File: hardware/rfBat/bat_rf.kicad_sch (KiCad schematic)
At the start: 98 parts, among them J1 USB_C_Receptacle_PowerOnly_6P, J2 Conn_01x02_Socket, J4 Conn_01x03, Q1 NMOS, Q2 PMOS, Q3 NMOS, Q4 KNY3406C, SW1 3*4*2.5MM_贴片4脚, SW3 SW_MEC_5E, U1 ESP32-C3-WROOM-02-N4, U2 IP2325_5M_WHJC, U3 SPX3819M5-L-3-3, U4 AMS1117

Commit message: update rfBat pcb
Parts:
- removed D1: BAT54C, Package_TO_SOT_SMD:SOT-23, symbol Diode:BAT54C
- removed Q1, Q3: NMOS, Package_TO_SOT_SMD:SOT-23, symbol Simulation_SPICE:NMOS
- removed Q2: PMOS, Package_TO_SOT_SMD:SOT-23, symbol Simulation_SPICE:PMOS
- removed SW3: SW_MEC_5E, bat_rf:SW-SMD_EVQPUD02K, symbol Switch:SW_MEC_5E
- removed TP12: TestPoint, TestPoint:TestPoint_Pad_D1.0mm, symbol Connector:TestPoint
- added D7: BAT54C, bat_rf:BAT54C, symbol bat_rf:BAT54C
- added Q2, Q5: AllPower__AP2300, bat_rf:SOT-23, symbol bat_rf:AllPower__AP2300
- added Q3: AO3401, bat_rf:AO3401, symbol bat_rf:AO3401
- added SW2: 3*4*2.5MM_贴片4脚, bat_rf:SW-SMD_4P-L4.2-W3.3-P2.15-LS5.1, symbol bat_rf:3*4*2.5MM_贴片4脚
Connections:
- net +3V3: now also Q3.2 (S); no longer R16.1
- net GNDD: now also R11.1, Q2.2 (S), SW2.4
- net GNDPWR: now also Q5.2 (S); no longer R11.1
- net KEY: now also D7.1 (A)
- net POWER_EN: now also Q2.1 (G)
- net VCC: now also R16.1, Q3.3 (D)
- net at R8.2: now also D7.2 (A), Q2.3 (D), Q3.1 (G)
- net at R6.2, R7.2: now also Q5.1 (G)
- net at BZ1.2 (+), D5.2 (A): now also Q5.3 (D)
- new net: D7.3 (C), SW2.1
- no-connect marks 5 -> 7
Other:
- moved on the sheet: D6, R16

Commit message: update rfBat pcb
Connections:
- no-connect marks 7 -> 8
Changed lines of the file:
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@@
 		(at 218.44 44.45)
 	)
+	(no_connect
+		(at 45.72 177.8)
+	)
 	(wire
 		(pts
@@
 		(on_board yes)
 		(dnp no)
-		(fields_autoplaced yes)
 		(property "Reference" "U3"
 			(at 160.02 44.45 0)
@@
 		(on_board yes)
 		(dnp no)
-		(fields_autoplaced yes)
 		(property "Reference" "C4"
 			(at 139.7 27.9399 0)

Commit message: update rfBat firmware
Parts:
- removed BZ1: Buzzer, bat_rf:BUZ-SMD_FUET-9045, symbol Device:Buzzer
- removed C15: 10u, Capacitor_SMD:C_0805_2012Metric_Pad1.18x1.45mm_HandSolder, symbol Device:C_Small
- removed C9: 100n, Capacitor_SMD:C_0603_1608Metric_Pad1.08x0.95mm_HandSolder, symbol Device:C_Small
- removed Q3: AO3401, bat_rf:AO3401, symbol bat_rf:AO3401
- removed SW1: 3*4*2.5MM_贴片4脚, bat_rf:SW-SMD_4P-L4.2-W3.3-P2.15-LS5.1, symbol bat_rf:3*4*2.5MM_贴片4脚
- removed TP8: TestPoint, TestPoint:TestPoint_Pad_D1.0mm, symbol Connector:TestPoint
- removed U3: SPX3819M5-L-3-3, Package_TO_SOT_SMD:SOT-23-5, symbol Regulator_Linear:SPX3819M5-L-3-3
- added Q1: AON7403, bat_rf:PQFN-8_L3.1-W3.1-P0.65-LS3.3-BL, symbol bat_rf:AON7403
- added SW3: TS-1199A-B-B, Button_Switch_SMD:SW_SPST_B3U-1000P, symbol espController:TS-1199A-B-B
- added U5: MLT-8530-5V, bat_rf:BUZ-SMD_4P-L8.5-W8.5-TL, symbol bat_rf:MLT-8530-5V
- added U6: TPLP2992IM5X-3.3, bat_rf:SOT-23-5_L2.9-W1.6-P0.95-LS2.8-BL, symbol bat_rf:TPLP2992IM5X-3.3
- C37: value 2.2u -> 100n
- C7: value 10n -> 1u
- C8: value 10u -> 1u; footprint Capacitor_SMD:C_0805_2012Metric_Pad1.18x1.45mm_HandSolder -> Capacitor_SMD:C_0603_1608Metric_Pad1.08x0.95mm_HandSolder
- D13: value LED -> B_LED; footprint LED_SMD:LED_0402_1005Metric_Pad0.77x0.64mm_HandSolder -> LED_SMD:LED_0603_1608Metric_Pad1.05x0.95mm_HandSolder
- D2, D6: footprint LED_SMD:LED_0402_1005Metric_Pad0.77x0.64mm_HandSolder -> LED_SMD:LED_0603_1608Metric_Pad1.05x0.95mm_HandSolder
- D3: value LED -> G_LED; footprint LED_SMD:LED_0402_1005Metric_Pad0.77x0.64mm_HandSolder -> LED_SMD:LED_0603_1608Metric_Pad1.05x0.95mm_HandSolder
- D4: value LED -> Y_LED; footprint LED_SMD:LED_0402_1005Metric_Pad0.77x0.64mm_HandSolder -> LED_SMD:LED_0603_1608Metric_Pad1.05x0.95mm_HandSolder
- R13, R15, R5: value 1k -> 3k
- R3: value 100R -> 3k
- R9: value 7m -> 7.5m
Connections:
- net +3V3: now also C12.1, C13.1, R12.2, R16.1, R4.2, TP1.1, U1.1 (3V3), U6.5 (VOUT); no longer R8.1
- net +5V: now also R8.1, Q1.1 (S), Q1.2 (S), Q1.3 (S); no longer C11.2, C14.2, C17.2, C30.2, C31.2, C32.2, C33.2, C34.2, C35.2, C36.2, C5.2, C6.2, D5.1 (K), LED1.3 (VDD), LED10.3 (VDD), LED11.3 (VDD), LED12.3 (VDD), LED2.3 (VDD), LED3.3 (VDD), LED4.3 (VDD), LED5.3 (VDD), LED6.3 (VDD), LED7.3 (VDD), LED8.3 (VDD), LED9.3 (VDD)
- net EN: now also SW3.2
- net GNDD: now also SW3.1, U6.2 (GND)
- net VCC: now also C11.2, C14.2, C17.2, C30.2, C31.2, C32.2, C33.2, C34.2, C35.2, C36.2, C5.2, C6.2, C7.1, D5.1 (K), LED1.3 (VDD), LED10.3 (VDD), LED11.3 (VDD), LED12.3 (VDD), LED2.3 (VDD), LED3.3 (VDD), LED4.3 (VDD), LED5.3 (VDD), LED6.3 (VDD), LED7.3 (VDD), LED8.3 (VDD), LED9.3 (VDD), Q1.5 (D), Q1.6 (D), Q1.7 (D), Q1.8 (D), U5.1 (+), U6.1 (VIN), U6.3 (EN); no longer C12.1, C13.1, R12.2, R16.1, R4.2, TP1.1, U1.1 (3V3)
- net at D7.2 (A), Q2.3 (D), R8.2: now also Q1.4 (G)
- net at D5.2 (A), Q5.3 (D): now also U5.2 (-)
- no-connect marks 8 -> 9
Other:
- moved on the sheet: C1, C2, C3, C4, C8, D5, D6, D7, Q2, Q5, R11, R16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

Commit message: update pcb
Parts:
- removed C7, C8: 1u, Capacitor_SMD:C_0603_1608Metric_Pad1.08x0.95mm_HandSolder, symbol Device:C_Small
- removed U6: TPLP2992IM5X-3.3, bat_rf:SOT-23-5_L2.9-W1.6-P0.95-LS2.8-BL, symbol bat_rf:TPLP2992IM5X-3.3
- added C15, C9: 1u, Capacitor_SMD:C_0603_1608Metric_Pad1.08x0.95mm_HandSolder, symbol Device:C
- added U7: XC6220B331MR, Package_TO_SOT_SMD:SOT-23-5, symbol Regulator_Linear:XC6220B331MR
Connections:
- net +3V3: now also C15.1, U7.5 (VOUT)
- net VCC: now also C9.1, U7.1 (VIN), U7.3 (CE)
- new net GND: C15.2, C9.2, U7.2 (GND)
- no-connect marks 9 -> 8

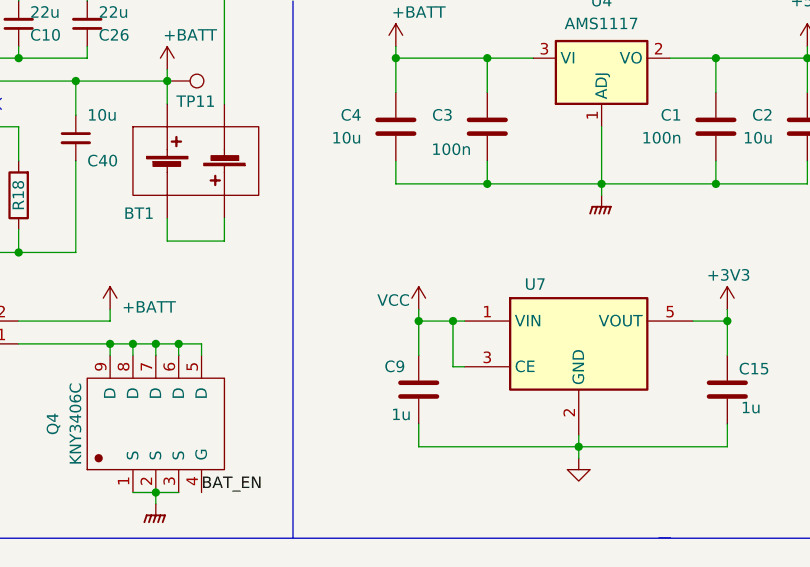
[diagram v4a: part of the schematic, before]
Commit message: update controller firmware
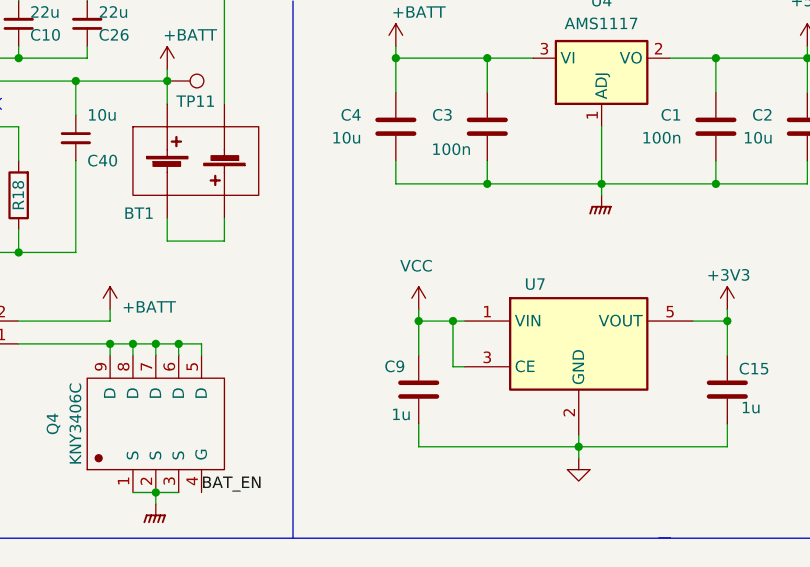
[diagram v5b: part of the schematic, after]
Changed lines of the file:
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@@
 		)
 		(property "Value" "VCC"
-			(at 144.526 49.784 0)
+			(at 147.066 45.974 0)
 			(effects
 				(font

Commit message: update rfBat pcb
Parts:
- removed Q1: AON7403, bat_rf:PQFN-8_L3.1-W3.1-P0.65-LS3.3-BL, symbol bat_rf:AON7403
- removed Q4: KNY3406C, bat_rf:PDFN-8_L4.9-W5.8-P1.27-LS6.1-BL, symbol bat_rf:KNY3406C
- removed TP1, TP2, TP3, TP4, TP5, TP6: TestPoint, TestPoint:TestPoint_Pad_D1.0mm, symbol Connector:TestPoint
- added J3: Conn_01x06, kicadLib:CONN-SMD_6P-P1.00_XYECONN_XY-SH1.0-6A61, symbol Connector_Generic:Conn_01x06
- added Q1: Q_PMOS_GDS, Package_TO_SOT_SMD:TO-252-2, symbol Device:Q_PMOS_GDS
- added R17: 500R, Resistor_SMD:R_0603_1608Metric_Pad0.98x0.95mm_HandSolder, symbol Device:R
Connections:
- net +3V3: now also J3.6 (Pin_6)
- net +5V: now also C11.2, C14.2, C17.2, C30.2, C31.2, C32.2, C33.2, C34.2, C35.2, C36.2, C5.2, C6.2, C9.1, D5.1 (K), LED1.3 (VDD), LED10.3 (VDD), LED11.3 (VDD), LED12.3 (VDD), LED2.3 (VDD), LED3.3 (VDD), LED4.3 (VDD), LED5.3 (VDD), LED6.3 (VDD), LED7.3 (VDD), LED8.3 (VDD), LED9.3 (VDD), U5.1 (+), U7.1 (VIN), U7.3 (CE); no longer R8.1
- net +BATT: now also R8.1, Q1.2 (D); no longer C3.1, C4.1, J2.2 (Pin_2), U4.3 (VI)
- net EN: now also J3.3 (Pin_3)
- net GNDD: now also J3.1 (Pin_1)
- net GNDPWR: now also J2.1 (Pin_1), R17.1; no longer Q5.2 (S)
- net IO9: now also J3.2 (Pin_2)
- net RXD: now also J3.4 (Pin_4)
- net TXD: now also J3.5 (Pin_5)
- net VCC: now also C3.1, C4.1, J2.2 (Pin_2), U4.3 (VI), Q1.3 (S); no longer C11.2, C14.2, C17.2, C30.2, C31.2, C32.2, C33.2, C34.2, C35.2, C36.2, C5.2, C6.2, C9.1, D5.1 (K), LED1.3 (VDD), LED10.3 (VDD), LED11.3 (VDD), LED12.3 (VDD), LED2.3 (VDD), LED3.3 (VDD), LED4.3 (VDD), LED5.3 (VDD), LED6.3 (VDD), LED7.3 (VDD), LED8.3 (VDD), LED9.3 (VDD), U5.1 (+), U7.1 (VIN), U7.3 (CE)
- net at D7.2 (A), Q2.3 (D), R8.2: now also Q1.1 (G)
- net BAT_EN: no longer names the net of U1.4 (IO5)
- new net: Q5.2 (S), R17.2
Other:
- moved on the sheet: C12, C13, C16, J2, R12, R4, U1

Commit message: update rfbat pcb
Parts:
- removed J2: Conn_01x02_Socket, bat_rf:CONN-TH_XT30U-F, symbol Connector:Conn_01x02_Socket
- removed TP11: TestPoint, TestPoint:TestPoint_Pad_D1.0mm, symbol Connector:TestPoint
- added J2, J5: Conn_01x01_Pin, TestPoint:TestPoint_Pad_D4.0mm, symbol Connector:Conn_01x01_Pin
- added TP1: TestPoint, TestPoint:TestPoint_Pad_D1.0mm, symbol Connector:TestPoint
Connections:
- net GND is gone; now on net GNDPWR: C15.2, C9.2, U7.2 (GND)
- net +3V3: now also J3.3 (Pin_3); no longer J3.6 (Pin_6)
- net EN: now also J3.2 (Pin_2); no longer J3.3 (Pin_3)
- net GNDD: now also J3.6 (Pin_6), TP1.1; no longer J3.1 (Pin_1)
- net GNDPWR: now also J5.1 (Pin_1)
- net IO9: now also J3.1 (Pin_1); no longer J3.2 (Pin_2)
- net RXD: now also J3.5 (Pin_5); no longer J3.4 (Pin_4)
- net TXD: now also J3.4 (Pin_4); no longer J3.5 (Pin_5)
- net VCC: now also J2.1 (Pin_1)
- no-connect marks 8 -> 9
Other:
- moved on the sheet: SW3

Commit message: update pcn
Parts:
- removed C1, C3: 100n, Capacitor_SMD:C_0603_1608Metric_Pad1.08x0.95mm_HandSolder, symbol Device:C
- removed C2, C4: 10u, Capacitor_SMD:C_0805_2012Metric_Pad1.18x1.45mm_HandSolder, symbol Device:C
- removed D7: BAT54C, bat_rf:BAT54C, symbol bat_rf:BAT54C
- removed Q1: Q_PMOS_GDS, Package_TO_SOT_SMD:TO-252-2, symbol Device:Q_PMOS_GDS
- removed Q2: AllPower__AP2300, bat_rf:SOT-23, symbol bat_rf:AllPower__AP2300
- removed SW2: 3*4*2.5MM_贴片4脚, bat_rf:SW-SMD_4P-L4.2-W3.3-P2.15-LS5.1, symbol bat_rf:3*4*2.5MM_贴片4脚
- removed TP7: TestPoint, TestPoint:TestPoint_Pad_D1.0mm, symbol Connector:TestPoint
- removed U4: AMS1117, Package_TO_SOT_SMD:SOT-89-3_Handsoldering, symbol Regulator_Linear:AMS1117
- added D1, D7: 1N4148W, Diode_SMD:D_SOD-123, symbol Diode:1N4148W
- added Q1: NPN, symbol Simulation_SPICE:NPN
- added Q3: AO4407, bat_rf:SOP-8_L5.0-W4.0-P1.27-LS6.0-BL, symbol bat_rf:AO4407
- added R19: 100R, Resistor_SMD:R_0603_1608Metric_Pad0.98x0.95mm_HandSolder, symbol Device:R
- added R20: 1k, Resistor_SMD:R_0603_1608Metric_Pad0.98x0.95mm_HandSolder, symbol Device:R
- added R21: 10k, Resistor_SMD:R_0603_1608Metric_Pad0.98x0.95mm_HandSolder, symbol Device:R
- added SW1: 3*4*2.5MM_贴片4脚, bat_rf:SW-SMD_4P-L4.2-W3.3-P2.15-LS5.1, symbol bat_rf:3*4*2.5MM_贴片4脚
- added U3: MT2492, bat_rf:SOT-23-6_L2.9-W1.6-P0.95-LS2.8-BL, symbol bat_rf:MT2492
- R11: value 33k -> 1k
- R8: value 33k -> 10k
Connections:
- net +BATT: now also R8.2, Q3.1 (S), Q3.2 (S), Q3.3 (S); no longer R8.1
- net GNDD: now also C15.2, C9.2, U7.2 (GND); no longer R11.1
- net GNDPWR: now also Q1.3 (E), R21.2, SW1.4; no longer C15.2, C9.2, U7.2 (GND)
- net KEY: now also D1.2 (A)
- net POWER_EN: now also R20.1; no longer R11.2
- net VCC: now also Q3.5 (D), Q3.6 (D), Q3.7 (D), Q3.8 (D)
- new net: Q1.2 (B), R20.2, R21.1
- new net: Q3.4 (G), R19.2, R8.1
- new net: D1.1 (K), D7.1 (K), SW1.1
- new net K1: D7.2 (A), Q1.1 (C), R19.1
- no-connect marks 9 -> 7
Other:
- moved on the sheet: C11, C12, C13, C14, C15, C16, C17, C30, C31, C32, C33, C34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
